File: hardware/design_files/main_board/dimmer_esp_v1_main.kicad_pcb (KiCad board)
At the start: 4 copper layers, 44 x 48.1 mm, 54 parts, among them IC1 PEC11S-929K-S0015, J1 Screw_Terminal_01x03, J2 SM05B-SRSS-TB_LF__SN_, J3 Conn_01x02, K1 FTR-LYCA005Y, Q1 BC817, SW1 Commission, SW2 Toggle, SW3 Reset, U1 SGM2212-3.3XKC3G/TR, U2 USB TYPE-C 16PLT-H10.0, U3 SN74LV1T125DBVR, U4 ESP32-C6-MINI

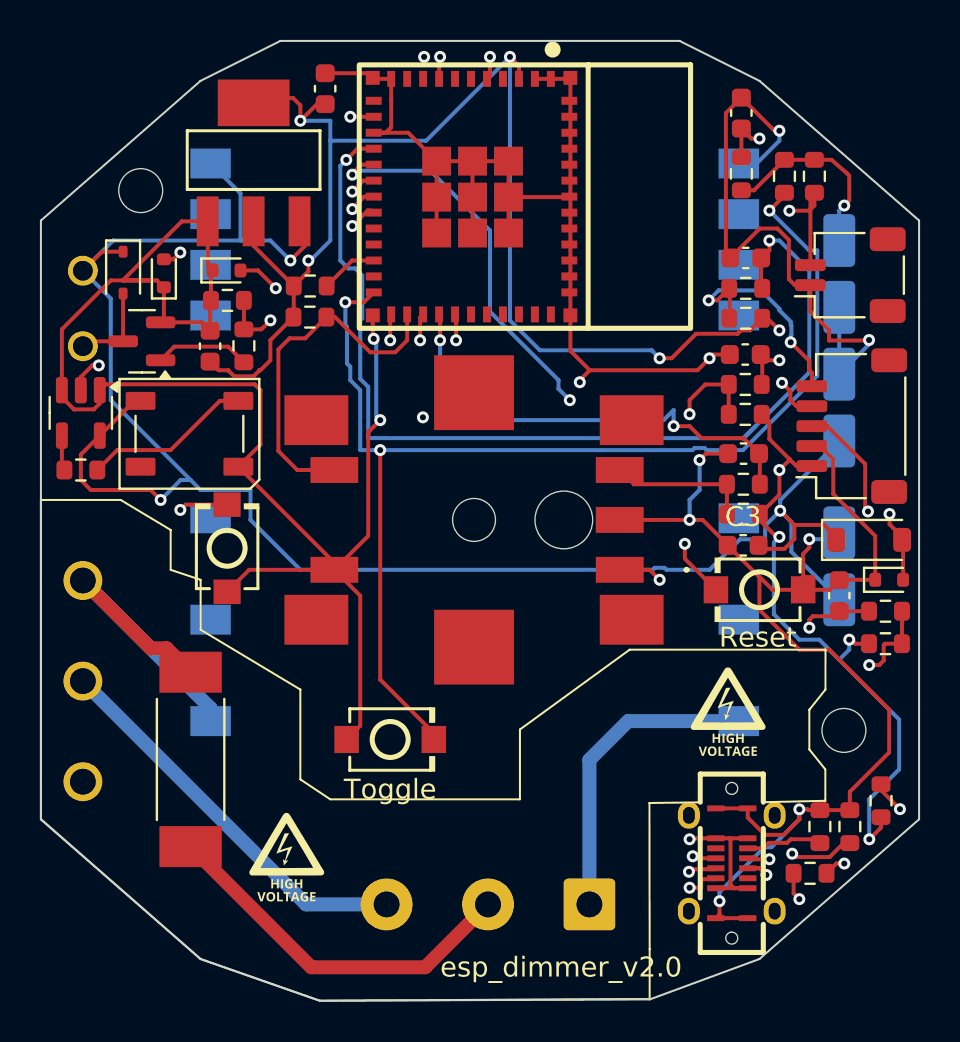
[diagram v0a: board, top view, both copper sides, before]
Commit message: Hardware: Smaller fixes
* Missing power flags
* Add missing bypass cap for LED
* Fix labels
* Add test points for GPIO9, TX, RX, and ground
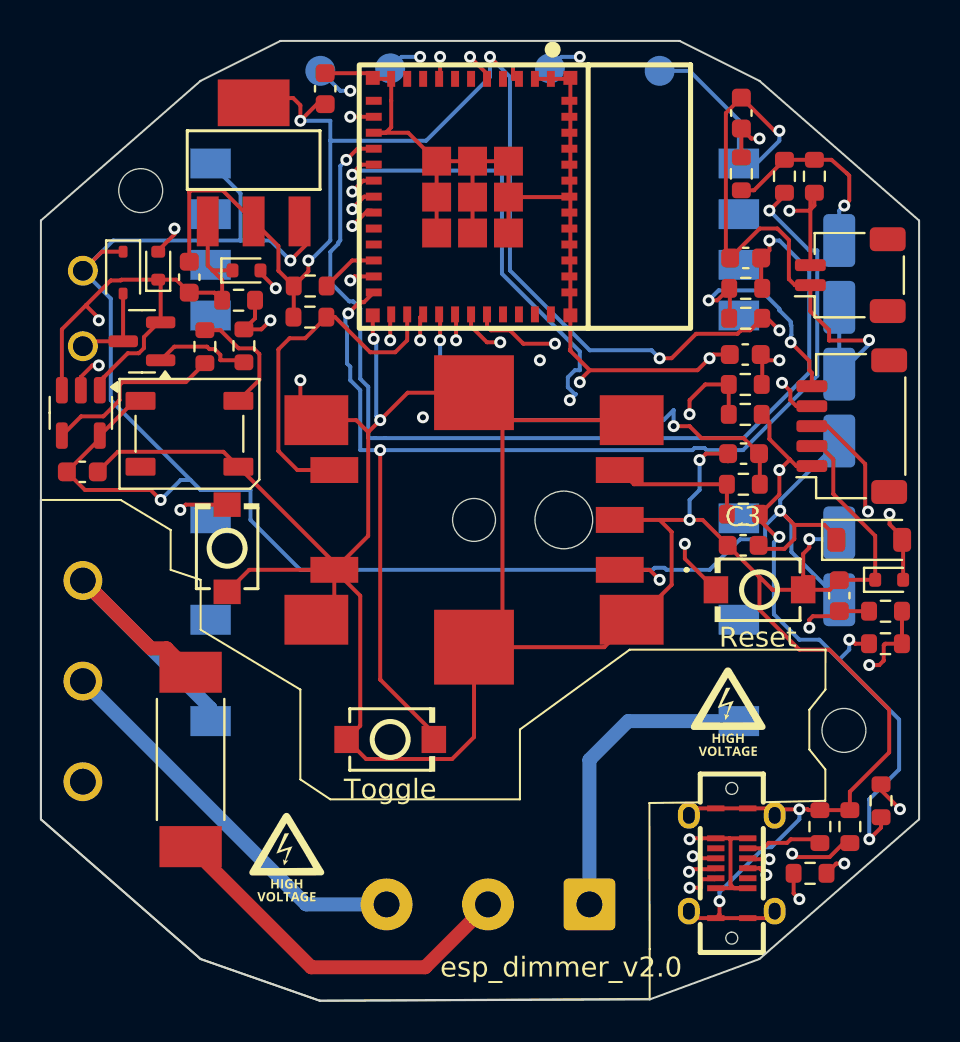
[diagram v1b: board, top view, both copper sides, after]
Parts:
- added C9: 0.1uF/50V(10%), Capacitor_SMD:C_0603_1608Metric, F.Cu at (147.6, 58.6)
- added TP1: GPIO9, TestPoint:TestPoint_Pad_D1.5mm, B.Cu at (159.5, 38.5)
- added TP2: TX, TestPoint:TestPoint_Pad_D1.5mm, B.Cu at (171.0, 38.4)
- added TP3: RX, TestPoint:TestPoint_Pad_D1.5mm, B.Cu at (163.0, 38.4)
- added TP4: GND, TestPoint:TestPoint_Pad_D1.5mm, B.Cu at (176.5, 38.5)
- moved R20 8.77 mm to (153.7, 52.3), turned to 90 degrees
- moved C5 3.61 mm to (152.9, 48.8), turned to 90 degrees
- moved D5 1.00 mm to (155.8, 48.5)
- moved R6 0.56 mm to (155.4, 50.0)
- moved D3 0.47 mm to (151.4, 48.3)
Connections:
- net /D01 renamed /GPIO01
- net /D02_relay renamed /GPIO02_relay
- net /D06 renamed /GPIO06
- net /D07 renamed /GPIO07
- net /D12 renamed /GPIO12
- net /D13 renamed /GPIO13
- net /D14 renamed /GPIO14
- net /D18 renamed /GPIO18
- net /D19 renamed /GPIO19
- net /D20 renamed /GPIO20
- net /D21 renamed /GPIO21
- net /D22 renamed /GPIO22
- net /D23_commission renamed /GPIO23_commission
- IC1 pad MP1: unconnected-(IC1-PadMP1) -> GND
- IC1 pad MP2: unconnected-(IC1-PadMP2) -> GND
- IC1 pad MP3: unconnected-(IC1-PadMP3) -> GND
- IC1 pad MP4: unconnected-(IC1-PadMP4) -> GND
- IC1 pad MP5: unconnected-(IC1-PadMP5) -> GND
- IC1 pad MP6: unconnected-(IC1-PadMP6) -> GND
- U2 pad 0: unconnected-(U2-EH-Pad0) -> GND
- U4 pad 23: /D09 -> /GPIO09_boot
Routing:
- net GND: track 263.3 -> 340.2 mm, vias 11 -> 13
- net /UART_TXD: track 0.00 -> 21.8 mm, vias 0 -> 2
- net /UART_RXD: track 0.00 -> 20.1 mm, vias 0 -> 2
- net /GPIO09_boot: track 0.00 -> 15.3 mm, vias 0 -> 2
- net /GPIO02_relay: track 24.5 -> 34.7 mm, vias 3 -> 2
- net Net-(U3-Y): track 2.44 -> 9.77 mm
- net /GPIO07: track 33.8 -> 36.8 mm
- net /GPIO01: track 24.8 -> 21.9 mm
- net Net-(D6-DIN): track 8.50 -> 6.01 mm
- net /GPIO14: track 38.4 -> 40.7 mm
- net /GPIO12: track 80.6 -> 82.0 mm
- net /GPIO13: track 73.6 -> 72.7 mm
- net +5V: track 96.1 -> 96.9 mm
- net +3.3V: track 131.4 -> 132.0 mm
- net /GPIO06: track 51.1 -> 50.5 mm
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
